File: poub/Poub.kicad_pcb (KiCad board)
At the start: 4 copper layers, 73 x 57 mm, 25 parts, among them J1 Conn_01x04, J2 Conn_01x04, J4 Conn_01x02, Q1 S8550, U3 PCI_express_x1, U4 HX711

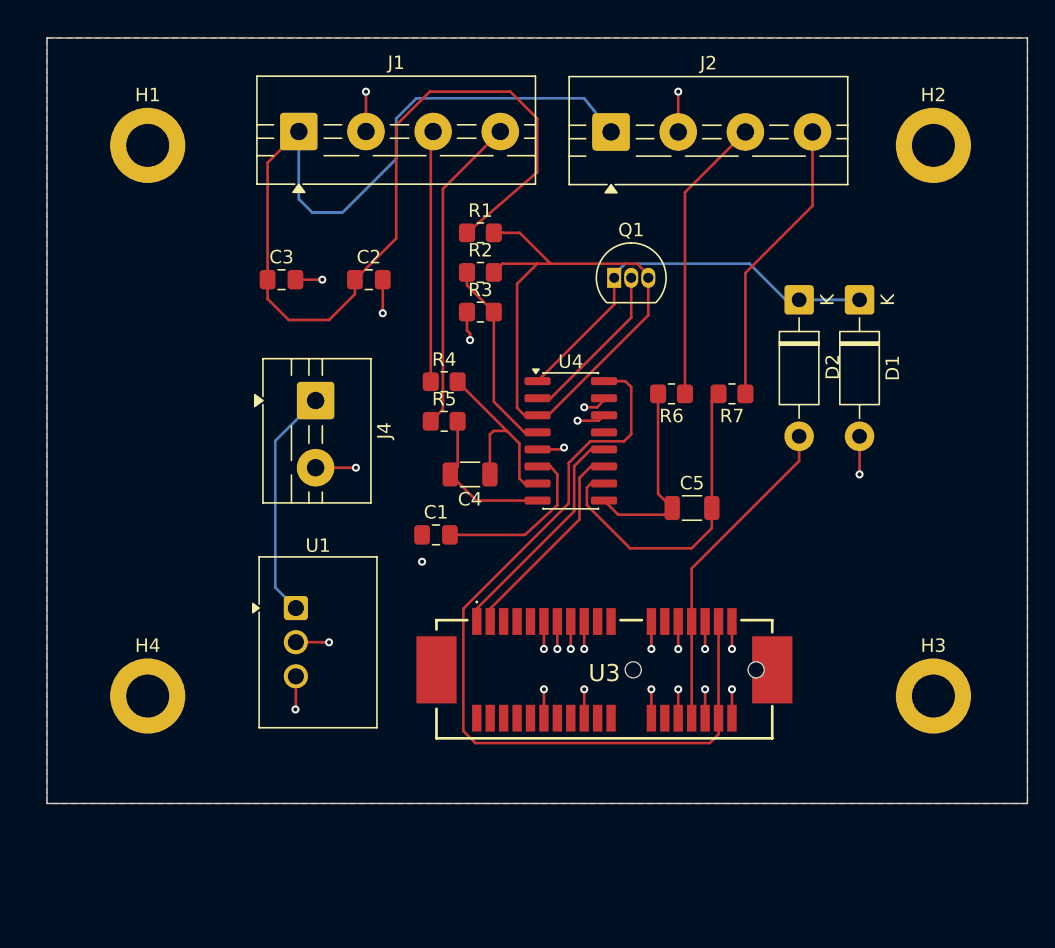
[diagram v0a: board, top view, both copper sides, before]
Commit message: Add files via upload
correction of some symbols and footprints
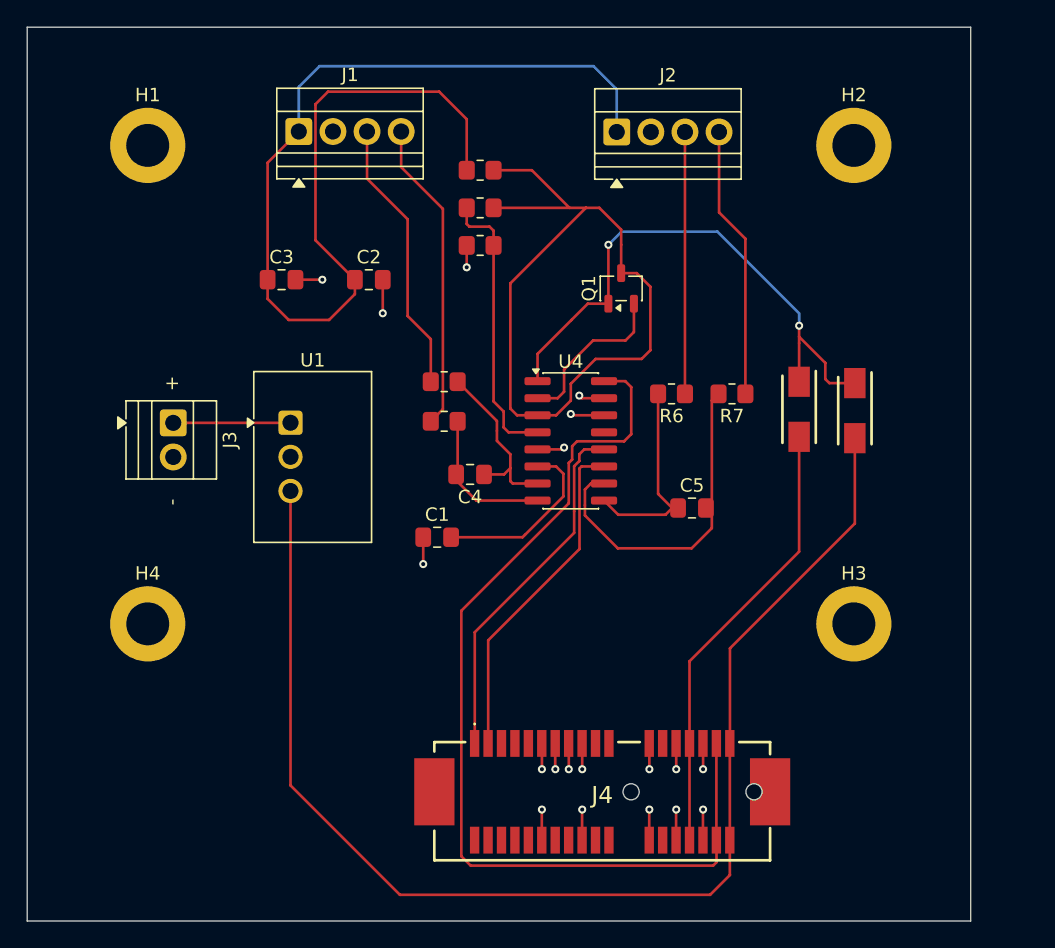
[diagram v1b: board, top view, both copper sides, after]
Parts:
- removed U3: PCI_express_x1, my_library_KiCad:10061913110CLF
- added J4: PCI_express_x1, lib_PCI_express_x1:10061913110CLF, F.Cu at (110.3, 93.8)
- C4, C5: footprint Capacitor_SMD:C_1206_3216Metric -> Capacitor_SMD:C_0805_2012Metric_Pad1.18x1.45mm_HandSolder
- D1, D2: value 1N5819 -> FM5817-W; footprint Diode_THT:D_DO-41_SOD81_P10.16mm_Horizontal -> lib_diode:DIOM5025X231N
- J1: value Conn_01x04 -> SensorA; footprint TerminalBlock:TerminalBlock_MaiXu_MX126-5.0-04P_1x04_P5.00mm -> TerminalBlock:TerminalBlock_Xinya_XY308-2.54-4P_1x04_P2.54mm_Horizontal
- J2: value Conn_01x04 -> SensorB; footprint TerminalBlock:TerminalBlock_MaiXu_MX126-5.0-04P_1x04_P5.00mm -> TerminalBlock:TerminalBlock_Xinya_XY308-2.54-4P_1x04_P2.54mm_Horizontal
- J3: renamed from J4; footprint TerminalBlock:TerminalBlock_MaiXu_MX126-5.0-02P_1x02_P5.00mm -> TerminalBlock:TerminalBlock_Xinya_XY308-2.54-2P_1x02_P2.54mm_Horizontal
- Q1: footprint Package_TO_SOT_THT:TO-92_Inline -> Package_TO_SOT_SMD:SOT-23-3
- moved U1 13.8 mm to (87.1, 65.7)
- moved J3 10.7 mm to (78.4, 65.7)
- moved D1 8.26 mm to (129.2, 64.8)
- moved D2 8.15 mm to (125.0, 64.7)
- moved H3 8.00 mm to (129.1, 80.6)
- moved H2 5.93 mm to (129.1, 45.0)
- moved H4 5.38 mm to (76.5, 80.6)
- moved R3 4.96 mm to (101.2, 52.5)
- moved R2 4.81 mm to (101.2, 49.6)
- moved R1 4.66 mm to (101.2, 46.9)
- moved Q1 0.95 mm to (111.8, 55.6), turned to 90 degrees
- moved J2 0.42 mm to (111.4, 44.0)
- moved C1 0.20 mm to (98.0, 74.2)
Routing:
- net 5V_local: track 9.51 -> 94.9 mm, vias 4 -> 0
- net Net-(Q1-C): track 44.7 -> 58.2 mm
- net 5V: track 30.0 -> 41.7 mm, vias 0 -> 2
- net 3.3V: track 62.5 -> 72.8 mm
- net SCK: track 15.6 -> 25.1 mm
- net Net-(J1-Pin_1): track 93.9 -> 84.5 mm
- net DOUT: track 17.3 -> 26.6 mm
- net GND: track 49.2 -> 40.0 mm, vias 23 -> 19
- net VBUS: track 24.3 -> 33.4 mm
- net Net-(J3-Pin_1): track 17.3 -> 8.73 mm
- net Net-(U4-VFB): track 14.7 -> 21.0 mm
- net Net-(U4-INA-): track 15.3 -> 13.3 mm
- net Net-(J1-Pin_3): track 18.7 -> 20.6 mm
- net Net-(J2-Pin_3): track 21.4 -> 19.5 mm
- net Net-(J2-Pin_4): track 21.6 -> 20.3 mm
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- removed copper zone on In2.Cu, net 5V_local
- removed copper zone on B.Cu, net GND
- removed copper zone on F.Cu, net GND
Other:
- board size 73 x 57 mm -> 70.2 x 66.5 mm
- board text added: "+"
- board text added: "-"
- board text removed: "${REFERENCE}"
